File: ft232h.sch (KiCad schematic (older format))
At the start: 32 parts, among them J3 USB_OTG, U14 FT232HL, U15 93LCxxBT-I/OT, X4 JTAG, Y3 ABLS2-12.000MHZ-D4Y-T

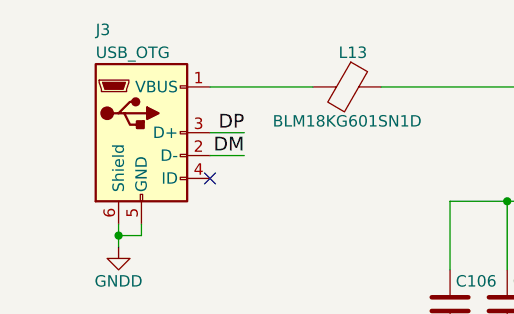
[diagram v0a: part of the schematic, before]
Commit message: Add logo, rev. GND testpoints etc in silkscreen.
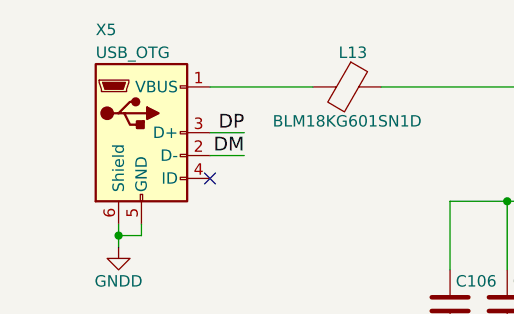
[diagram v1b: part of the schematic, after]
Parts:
- X4: footprint Pin_Headers:Pin_Header_Straight_1x05_Pitch2.00mm -> Pin_Headers:Pin_Header_Straight_1x05_Pitch1.27mm
- renumbered J3 to X5
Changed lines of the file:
@@
 	1050 3800 1050 3650
 $Comp
-L GNDD #PWR098
+L GNDD #PWR100
 U 1 1 59378D3B
 P 1450 3950
-F 0 "#PWR098" H 1450 3700 50  0001 C CNN
+F 0 "#PWR100" H 1450 3700 50  0001 C CNN
 F 1 "GNDD" H 1450 3800 50  0000 C CNN
 F 2 "" H 1450 3950 50  0001 C CNN
@@
 Connection ~ 1550 3200
 $Comp
-L USB_OTG J3
+L USB_OTG X5
 U 1 1 593793FD
 P 1200 2150
-F 0 "J3" H 1000 2600 50  0000 L CNN
+F 0 "X5" H 1000 2600 50  0000 L CNN
 F 1 "USB_OTG" H 1000 2500 50  0000 L CNN
 F 2 "Connectors:USB_Mini-B" H 1350 2100 50  0001 C CNN
@@
 $EndComp
 $Comp
-L GNDD #PWR099
+L GNDD #PWR104
 U 1 1 593794C0
 P 3900 4700
-F 0 "#PWR099" H 3900 4450 50  0001 C CNN
+F 0 "#PWR104" H 3900 4450 50  0001 C CNN
 F 1 "GNDD" H 3900 4550 50  0000 C CNN
 F 2 "" H 3900 4700 50  0001 C CNN
@@
 Connection ~ 4800 4650
 $Comp
-L GNDD #PWR0100
+L GNDD #PWR99
 U 1 1 59379721
 P 1100 2650
-F 0 "#PWR0100" H 1100 2400 50  0001 C CNN
+F 0 "#PWR99" H 1100 2400 50  0001 C CNN
 F 1 "GNDD" H 1100 2500 50  0000 C CNN
 F 2 "" H 1100 2650 50  0001 C CNN
@@
 	3050 2650 3050 2750
 $Comp
-L GNDD #PWR0101
+L GNDD #PWR103
 U 1 1 5937A2D8
 P 3050 3150
-F 0 "#PWR0101" H 3050 2900 50  0001 C CNN
+F 0 "#PWR103" H 3050 2900 50  0001 C CNN
 F 1 "GNDD" H 3050 3000 50  0000 C CNN
 F 2 "" H 3050 3150 50  0001 C CNN
@@
 $EndComp
 $Comp
-L GNDD #PWR0102
+L GNDD #PWR101
 U 1 1 5937D464
 P 2500 5250
-F 0 "#PWR0102" H 2500 5000 50  0001 C CNN
+F 0 "#PWR101" H 2500 5000 50  0001 C CNN
 F 1 "GNDD" H 2500 5100 50  0000 C CNN
 F 2 "" H 2500 5250 50  0001 C CNN
@@
 $EndComp
 $Comp
-L GNDD #PWR0103
+L GNDD #PWR102
 U 1 1 59380D23
 P 2700 4200
-F 0 "#PWR0103" H 2700 3950 50  0001 C CNN
+F 0 "#PWR102" H 2700 3950 50  0001 C CNN
 F 1 "GNDD" H 2700 4050 50  0000 C CNN
 F 2 "" H 2700 4200 50  0001 C CNN
@@
 F 0 "X4" H 7200 2850 50  0000 C CNN
 F 1 "JTAG" V 7300 2550 50  0000 C CNN
-F 2 "Pin_Headers:Pin_Header_Straight_1x05_Pitch2.00mm" H 7200 2550 50  0001 C CNN
+F 2 "Pin_Headers:Pin_Header_Straight_1x05_Pitch1.27mm" H 7200 2550 50  0001 C CNN
 F 3 "" H 7200 2550 50  0001 C CNN
 F 4 "NRPN201PAEN-RC" H 7200 2550 60  0001 C CNN "manf#"
@@
 	6400 2650 7000 2650
 $Comp
-L GNDD #PWR0104
+L GNDD #PWR105
 U 1 1 593E55E3
 P 6700 2800
-F 0 "#PWR0104" H 6700 2550 50  0001 C CNN
+F 0 "#PWR105" H 6700 2550 50  0001 C CNN
 F 1 "GNDD" H 6700 2650 50  0000 C CNN
 F 2 "" H 6700 2800 50  0001 C CNN
